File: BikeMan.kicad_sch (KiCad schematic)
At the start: 8 parts, among them J2 Screw_Terminal_01x08, J3 Screw_Terminal_01x08, J5 USB_A, J6 USB_A, J7 USB_A, J8 USB_A

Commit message: footprints
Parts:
- removed J5, J6, J7, J8: USB_A, symbol Connector:USB_A
- added J1, J2: USB_A_stacked, Connector_USB:USB_A_Wuerth_61400826021_Horizontal_Stacked, symbol symbols:USB_A_stacked
- R1: renamed from R33; footprint (none) -> Resistor_SMD:R_0805_2012Metric
- R2: renamed from R34; footprint (none) -> Resistor_SMD:R_0805_2012Metric
- renumbered J2 to J3, J3 to J4
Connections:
- net +5V: now also J1.5 (VBUS), J2.5 (VBUS)
- net D_{1}+: now also J1.6 (D-), J1.7 (D+)
- net D_{2}+: now also J1.1 (VBUS), J1.3 (D+)
- net D_{3}+: now also J2.6 (D-), J2.7 (D+)
- net D_{4}+: now also J2.1 (VBUS), J2.3 (D+)
- net GND: now also J1.4 (GND), J1.8 (GND), J1.9 (Shield), J2.4 (GND), J2.8 (GND), J2.9 (Shield)
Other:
- sheet ComputeModule_A ports: added SPI.CLK, SPI.MISO, SPI.MOSI, SPI.~CS_{CAN}, ~INT_{CAN}; removed none
- note removed: "Four USB ports is probably overkill"
- note removed: "TODO: connect to pi"

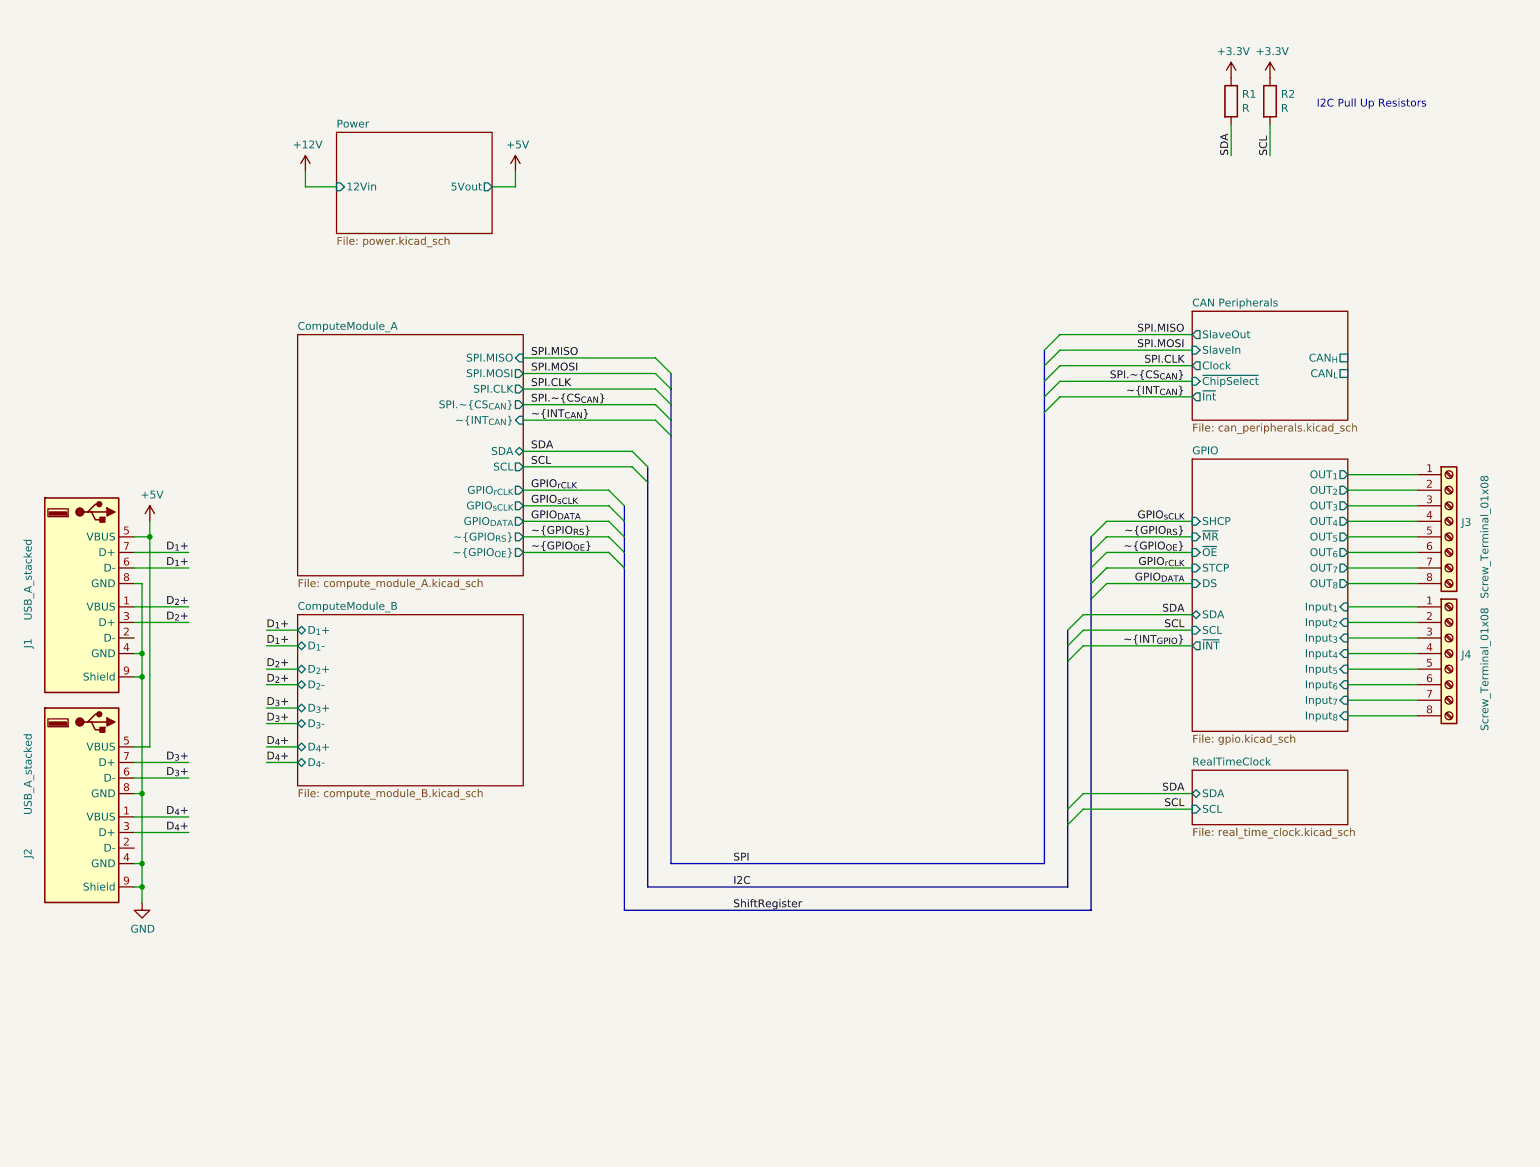
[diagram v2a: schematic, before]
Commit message: Adding footprints and step files for connectors
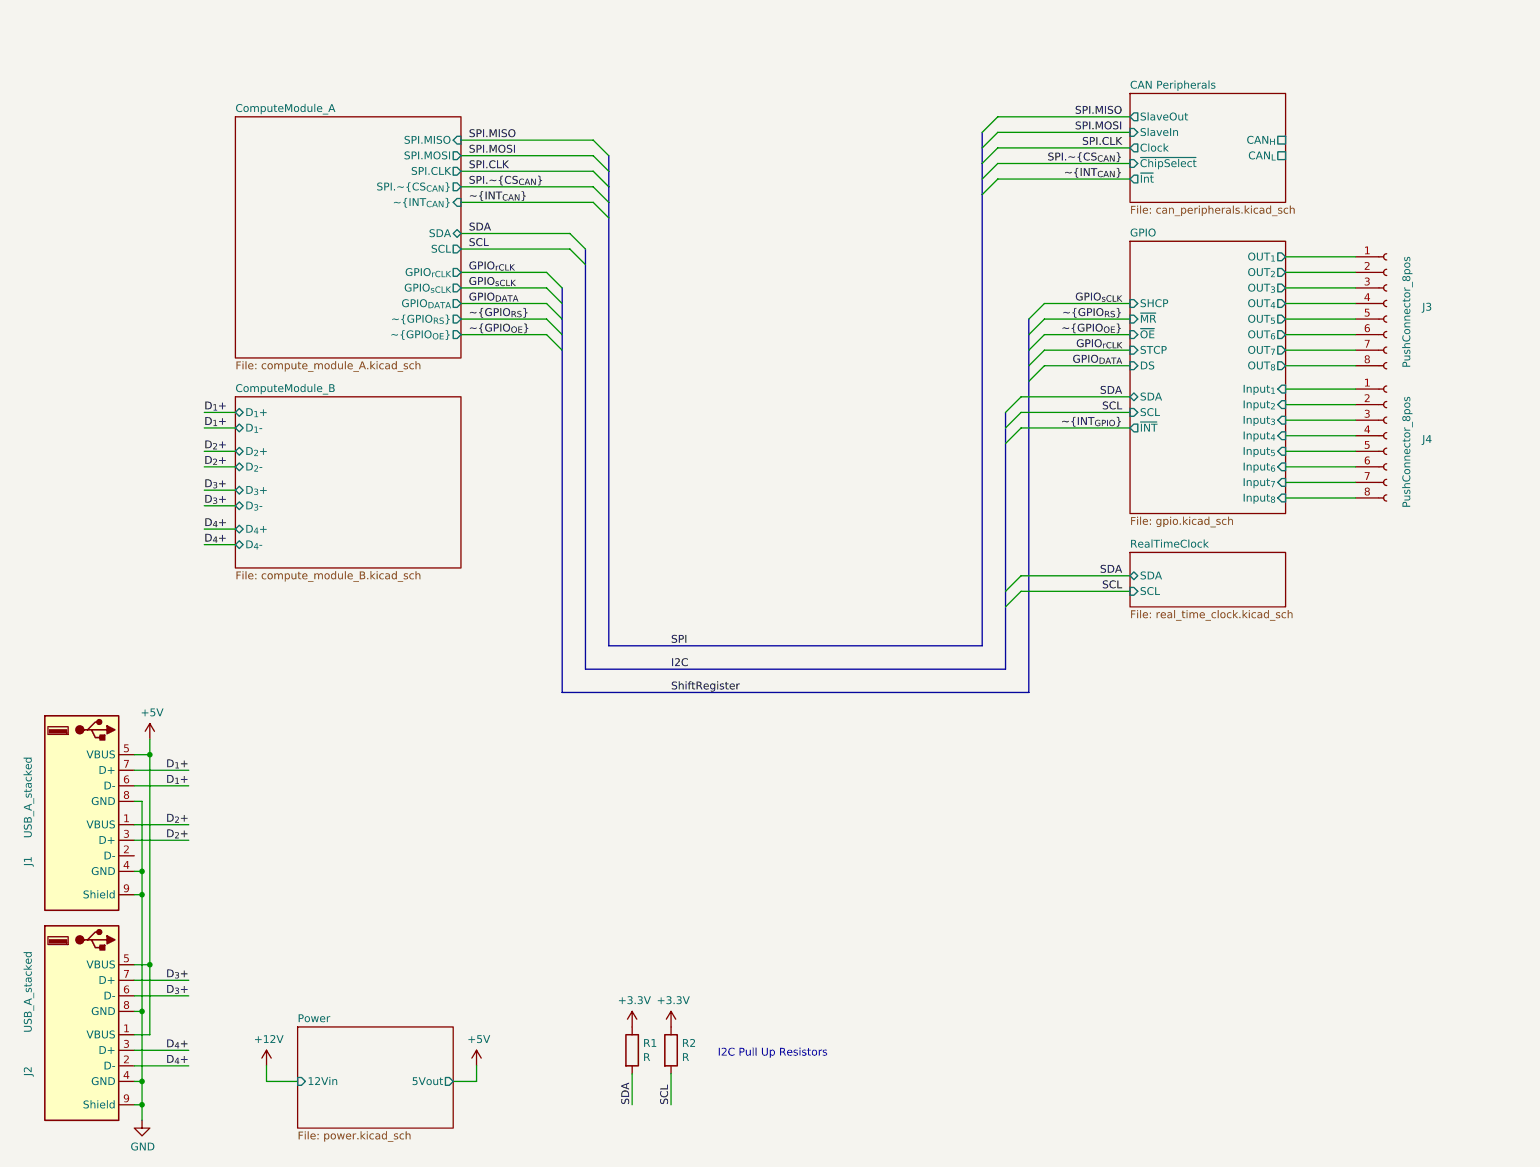
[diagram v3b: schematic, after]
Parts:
- removed J3, J4: Screw_Terminal_01x08, symbol Connector:Screw_Terminal_01x08
- added J3, J4: PushConnector_8pos, footprints:CUI_TBL004-508-08BE-2BE, symbol symbols:PushConnector_8pos
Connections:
- net +5V: now also J2.1 (VBUS)
- net D_{4}+: now also J2.2 (D-); no longer J2.1 (VBUS)
- net GPIO/Input_{1}: now also J4.1 (Pin_1)
- net GPIO/Input_{2}: now also J4.2 (Pin_2)
- net GPIO/Input_{3}: now also J4.3 (Pin_3)
- net GPIO/Input_{4}: now also J4.4 (Pin_4)
- net GPIO/Input_{5}: now also J4.5 (Pin_5)
- net GPIO/Input_{6}: now also J4.6 (Pin_6)
- net GPIO/Input_{7}: now also J4.7 (Pin_7)
- net GPIO/Input_{8}: now also J4.8 (Pin_8)
- net GPIO/OUT_{1}: now also J3.1 (Pin_1)
- net GPIO/OUT_{2}: now also J3.2 (Pin_2)
- net GPIO/OUT_{3}: now also J3.3 (Pin_3)
- net GPIO/OUT_{4}: now also J3.4 (Pin_4)
- net GPIO/OUT_{5}: now also J3.5 (Pin_5)
- net GPIO/OUT_{6}: now also J3.6 (Pin_6)
- net GPIO/OUT_{7}: now also J3.7 (Pin_7)
- net GPIO/OUT_{8}: now also J3.8 (Pin_8)
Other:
- moved on the sheet: J1, J2, R1, R2

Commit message: WIP
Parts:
- added D3: D_Schottky, symbol Device:D_Schottky
- added J5: Conn_01x04_Female, symbol Connector:Conn_01x04_Female
- added J9: Barrel_Jack, Connector_BarrelJack:BarrelJack_Horizontal, symbol symbols:Barrel_Jack
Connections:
- net +12V: now also D3.1 (K), J5.1 (Pin_1)
- net GND: now also J5.4 (Pin_4), J9.2
- new net: D3.2 (A), J9.1
- new net CAN_{H}: J5.2 (Pin_2)
- new net CAN_{L}: J5.3 (Pin_3)
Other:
- moved on the sheet: J1, J2, R1, R2

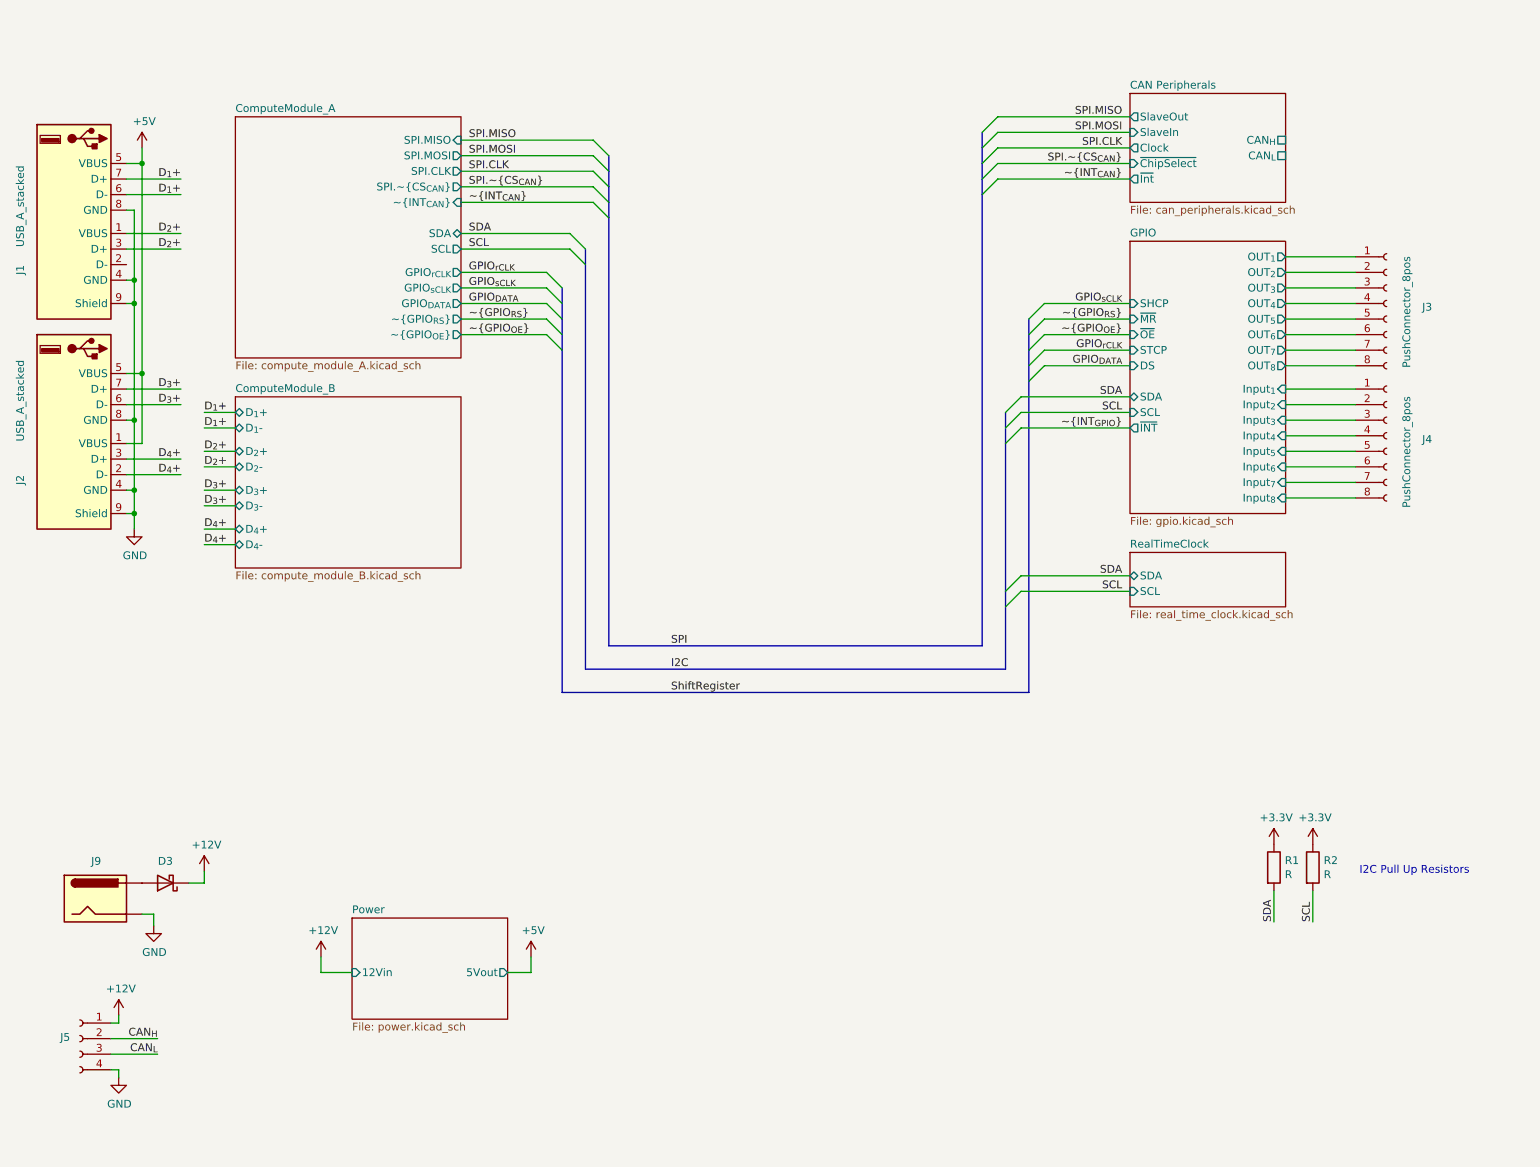
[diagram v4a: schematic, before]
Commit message: footprint assignments
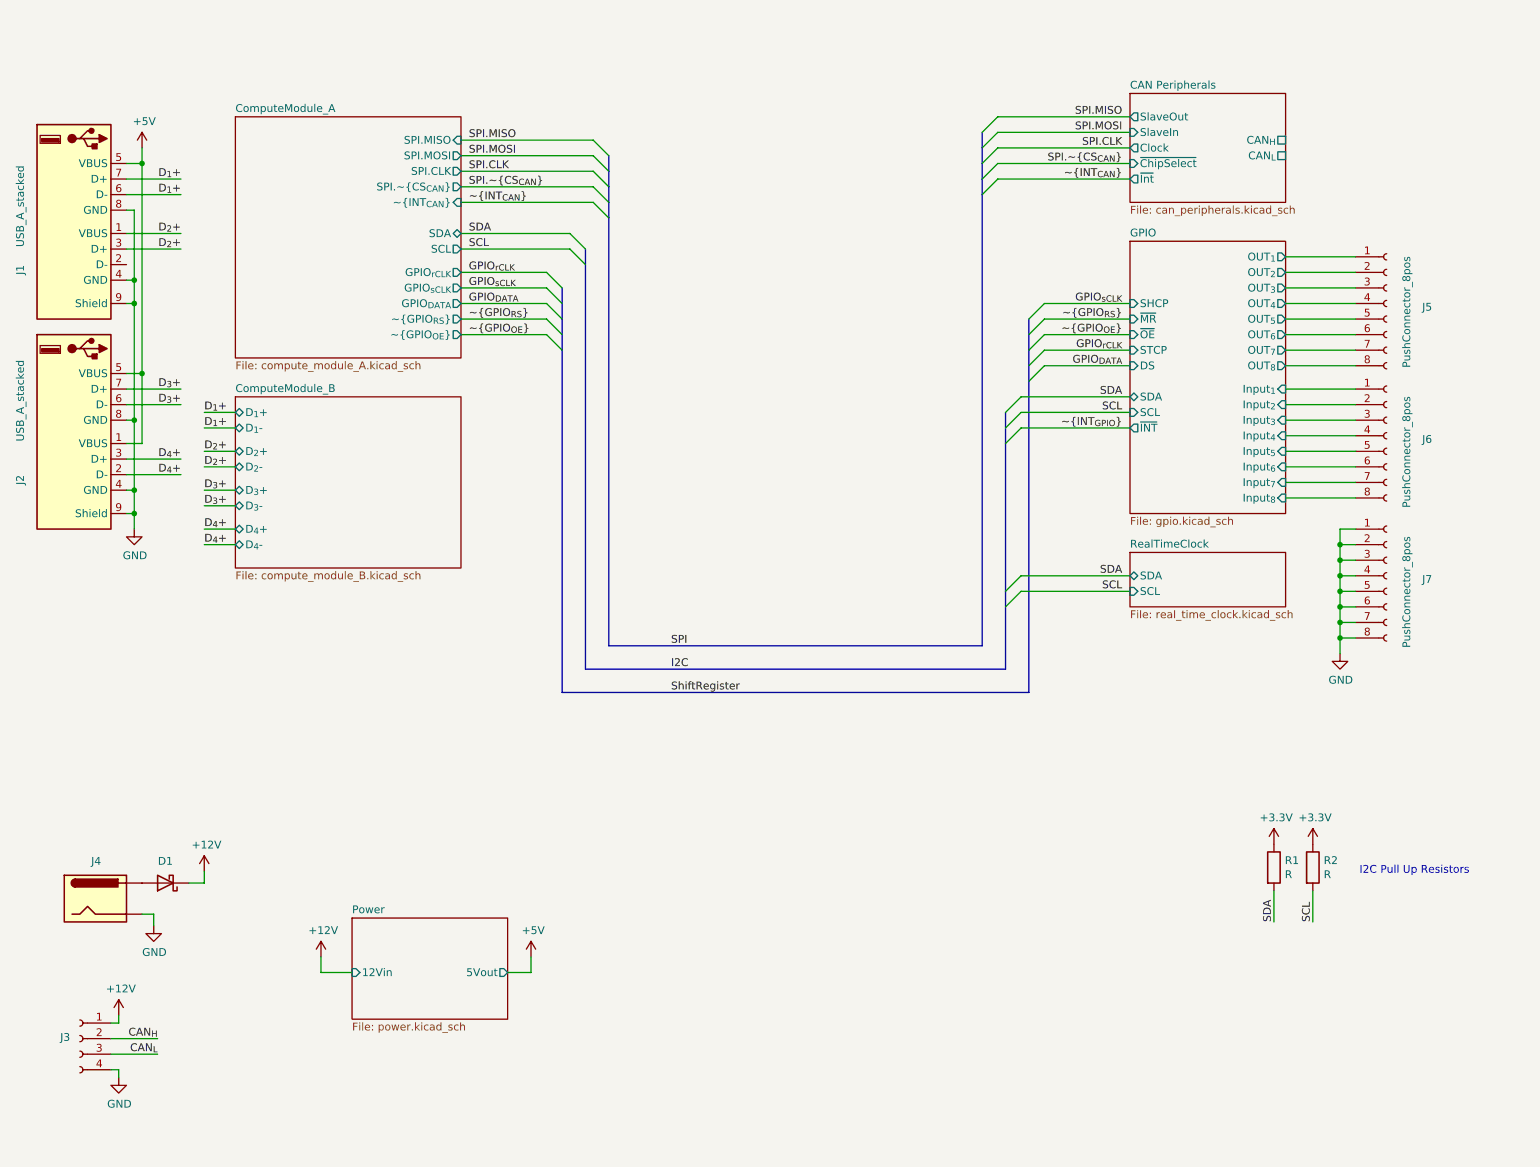
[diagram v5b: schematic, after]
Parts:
- added J7: PushConnector_8pos, footprints:CUI_TBL004-508-08BE-2BE, symbol symbols:PushConnector_8pos
- renumbered D3 to D1, J5 to J3, J9 to J4, J3 to J5, J4 to J6
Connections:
- net GND: now also J7.1 (Pin_1), J7.2 (Pin_2), J7.3 (Pin_3), J7.4 (Pin_4), J7.5 (Pin_5), J7.6 (Pin_6), J7.7 (Pin_7), J7.8 (Pin_8)
